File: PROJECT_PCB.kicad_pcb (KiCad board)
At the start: 4 copper layers, 88.2 x 56.4 mm, 84 parts, among them J1 SS-52400-003, J2 B2B-PH-K-S_LF__SN_, J3 GSD090012SEU, J4 Conn_01x04_Pin, J5 Conn_01x05_Pin, Q1 TEMT6000X01, Q2 BC817, Q3 BC817, U1 MCP73871, U2 USBLC6-2SC6, U3 ESP32-C3-WROOM-02, U4 CP2102N-Axx-xQFN20, U5 W25Q16JVSS, U6 BME280, U7 MAX4466EXK

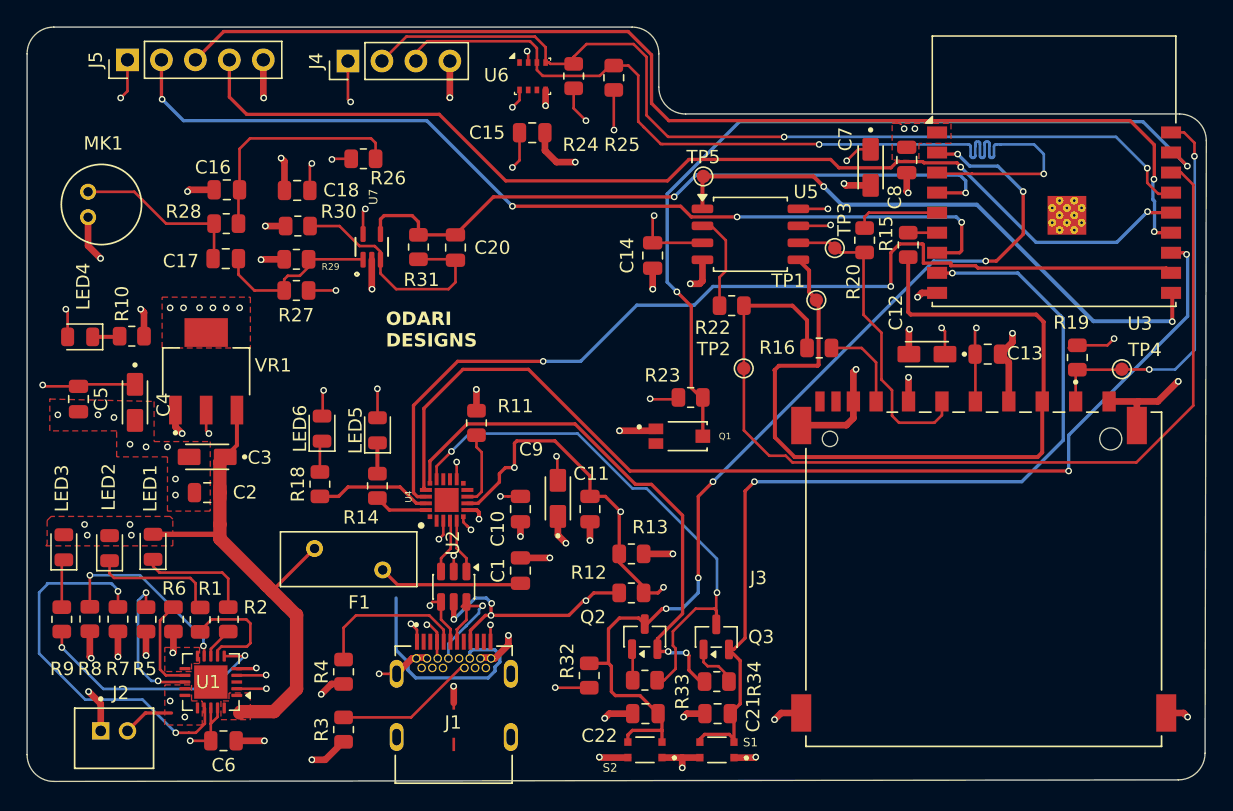
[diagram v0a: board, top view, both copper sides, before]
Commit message: update the symbol information for manufacturing suite
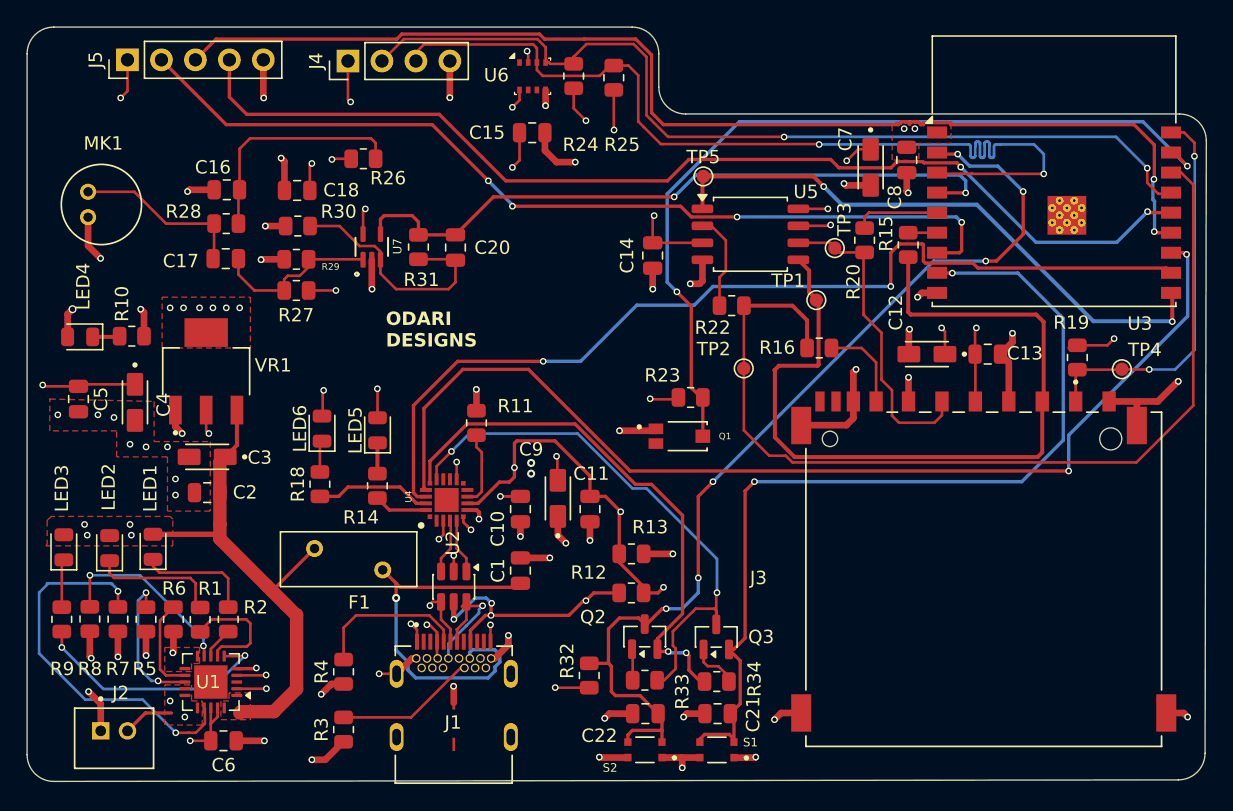
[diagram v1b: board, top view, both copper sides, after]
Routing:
- net /MCU_sheet/GPIO8: track 70.6 -> 69.0 mm
- net GND: track 129.7 -> 128.4 mm
- net Net-(J1-VBUSB1): track 27.8 -> 29.1 mm, vias 0 -> 1
- net /MCU_sheet/GPIO18: track 86.2 -> 87.1 mm
- net /VBUS: vias 5 -> 7
